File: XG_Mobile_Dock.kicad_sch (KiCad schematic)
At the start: 21 parts, among them J1 5-1775443-8, J17 8730, J2 20455-040E-76, J3 20455-040E-76, J4 3-2362375-4, J7 Conn_02x10_Odd_Even, J8 Conn_02x10_Odd_Even

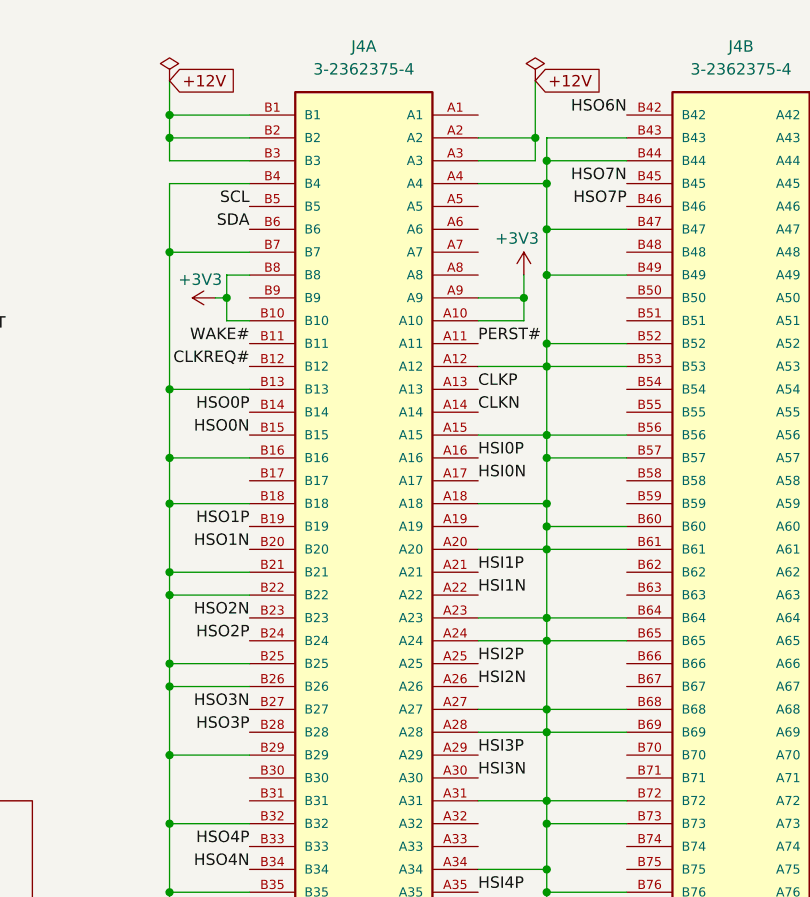
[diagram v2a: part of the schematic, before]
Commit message: Replace TH PCI-E slot with SMD
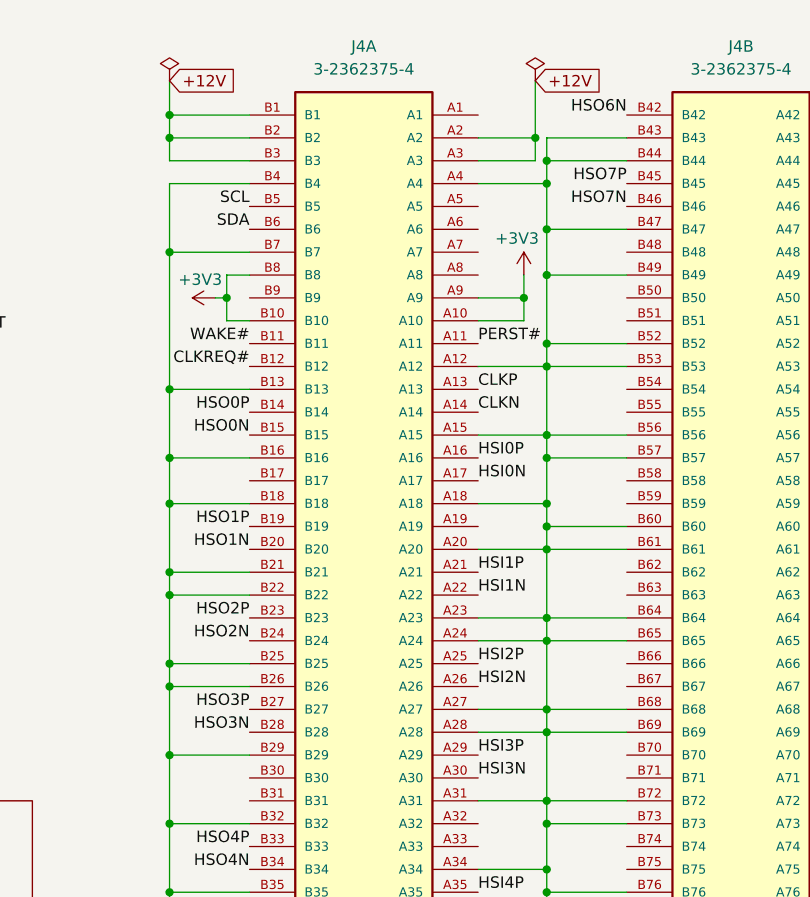
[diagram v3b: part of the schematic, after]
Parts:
- J4: footprint SAMTEC_PCIE-164-02-F-D-TH-TR:SAMTEC_PCIE-164-02-F-D-TH-TR -> 3113-113T:CONN-SMD_164P-P1.00-V_3133; LCSC C404116 -> C404104; Part_Number 3183-10203P1T -> 3113-113T
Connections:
- net HSO2N: now also J4.B24; no longer J4.B23
- net HSO2P: now also J4.B23; no longer J4.B24
- net HSO3N: now also J4.B28; no longer J4.B27
- net HSO3P: now also J4.B27; no longer J4.B28
- net HSO7N: now also J4.B46; no longer J4.B45
- net HSO7P: now also J4.B45; no longer J4.B46
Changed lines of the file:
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@@
 		)
 	)
-	(label "HSO3N"
+	(label "HSO3P"
 		(at 198.12 93.98 180)
 		(fields_autoplaced yes)
@@
 		)
 	)
-	(label "HSO2N"
+	(label "HSO2P"
 		(at 198.12 83.82 180)
 		(fields_autoplaced yes)
@@
 		)
 	)
-	(label "HSO3P"
+	(label "HSO3N"
 		(at 198.12 96.52 180)
 		(fields_autoplaced yes)
@@
 		)
 	)
-	(label "HSO7P"
+	(label "HSO7N"
 		(at 240.03 38.1 180)
 		(fields_autoplaced yes)
@@
 		)
 	)
-	(label "HSO7N"
+	(label "HSO7P"
 		(at 240.03 35.56 180)
 		(fields_autoplaced yes)
@@
 		)
 	)
-	(label "HSO2P"
+	(label "HSO2N"
 		(at 198.12 86.36 180)
 		(fields_autoplaced yes)
@@
 			)
 		)
-		(property "Footprint" "SAMTEC_PCIE-164-02-F-D-TH-TR:SAMTEC_PCIE-164-02-F-D-TH-TR"
+		(property "Footprint" "3113-113T:CONN-SMD_164P-P1.00-V_3133"
 			(at 252.73 78.74 0)
 			(effects
@@
 			)
 		)
-		(property "Part_Number" "3183-10203P1T"
+		(property "Part_Number" "3113-113T"
 			(at 252.73 78.74 0)
 			(effects
@@
 			)
 		)
-		(property "LCSC" "C404116"
+		(property "LCSC" "C404104"
 			(at 252.73 78.74 0)
 			(effects
@@
 			)
 		)
-		(property "Footprint" "SAMTEC_PCIE-164-02-F-D-TH-TR:SAMTEC_PCIE-164-02-F-D-TH-TR"
+		(property "Footprint" "3113-113T:CONN-SMD_164P-P1.00-V_3133"
 			(at 210.82 78.74 0)
 			(effects
@@
 			)
 		)
-		(property "Part_Number" "3183-10203P1T"
+		(property "Part_Number" "3113-113T"
 			(at 210.82 78.74 0)
 			(effects
@@
 			)
 		)
-		(property "LCSC" "C404116"
+		(property "LCSC" "C404104"
 			(at 210.82 78.74 0)
 			(effects

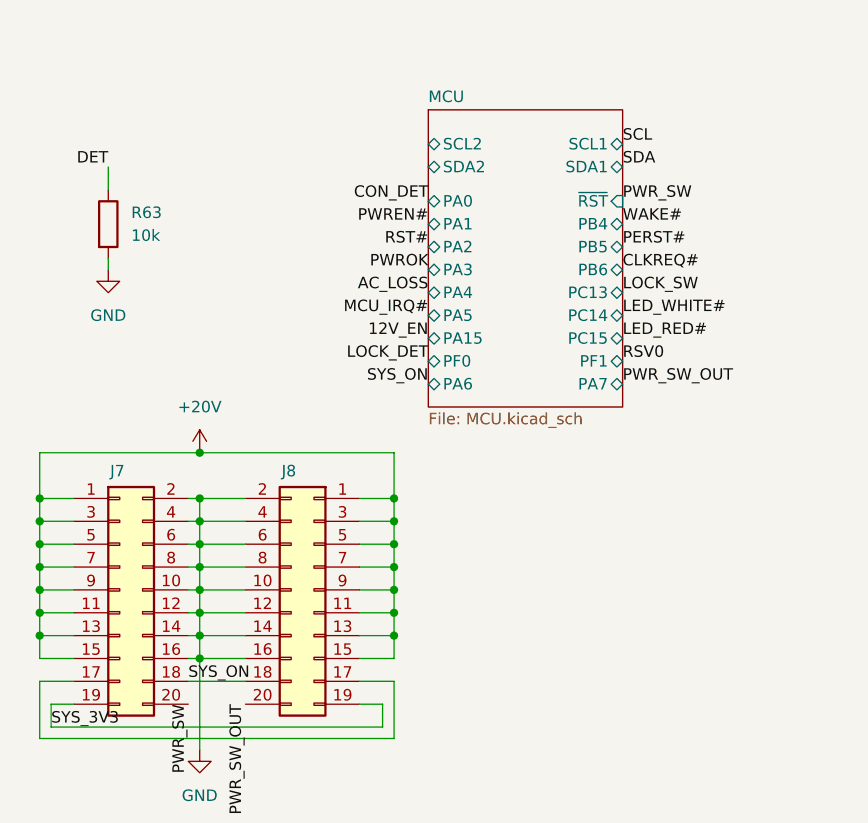
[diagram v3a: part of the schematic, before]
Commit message: Add external board detect pin to MCU
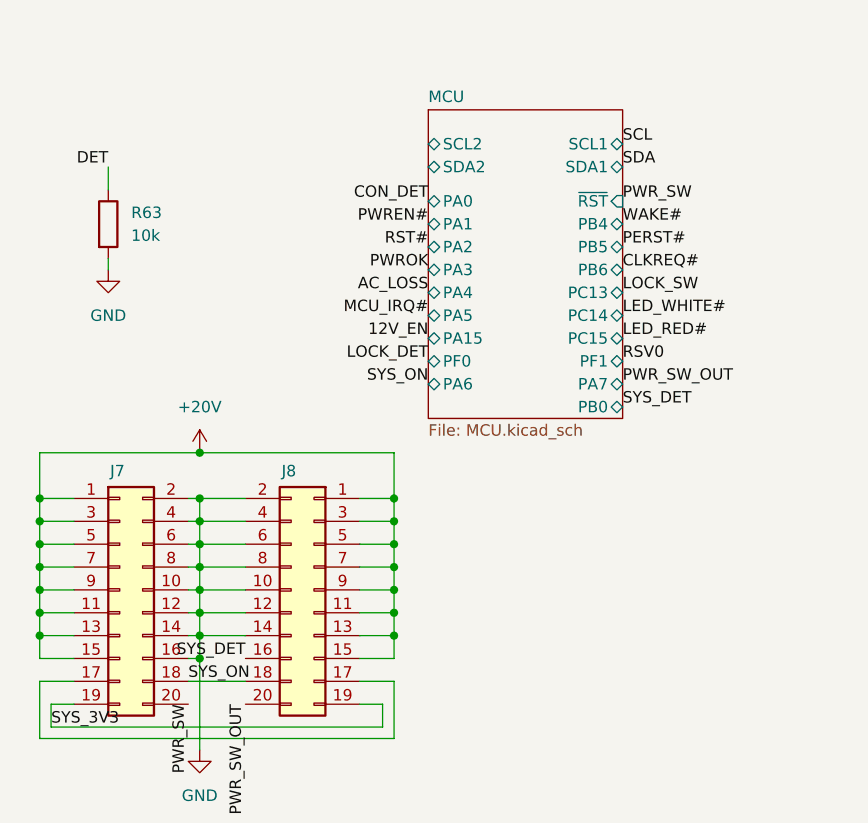
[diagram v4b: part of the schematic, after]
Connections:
- net GND: no longer J8.16 (Pin_16)
- new net SYS_DET: J8.16 (Pin_16)
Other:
- sheet MCU ports: added PB0; removed none
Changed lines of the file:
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@@
 	(wire
 		(pts
-			(xy 111.76 82.55) (xy 116.84 82.55)
-		)
-		(stroke
-			(width 0)
-			(type default)
-		)
-	)
-	(wire
-		(pts
 			(xy 46.99 67.31) (xy 46.99 74.93)
 		)
@@
 		)
 	)
+	(label "SYS_DET"
+		(at 116.84 82.55 180)
+		(fields_autoplaced yes)
+		(effects
+			(font
+				(size 1.27 1.27)
+			)
+			(justify right bottom)
+		)
+	)
 	(label "HSI6P"
 		(at 265.43 30.48 0)
@@
 		)
 	)
+	(label "SYS_DET"
+		(at 158.75 54.61 0)
+		(fields_autoplaced yes)
+		(effects
+			(font
+				(size 1.27 1.27)
+			)
+			(justify left bottom)
+		)
+	)
 	(label "HSO5P"
 		(at 198.12 119.38 180)
@@
 	(sheet
 		(at 137.16 21.59)
-		(size 21.59 33.02)
+		(size 21.59 34.29)
 		(fields_autoplaced yes)
 		(stroke
@@
 		)
 		(property "Sheetfile" "MCU.kicad_sch"
-			(at 137.16 55.1946 0)
+			(at 137.16 56.4646 0)
 			(effects
 				(font
@@
 			(effects
 				(font
+					(size 1.27 1.27)
+				)
+				(justify right)
+			)
+		)
+		(pin "PB0" bidirectional
+			(at 158.75 54.61 0)
+			(effects
+				(font

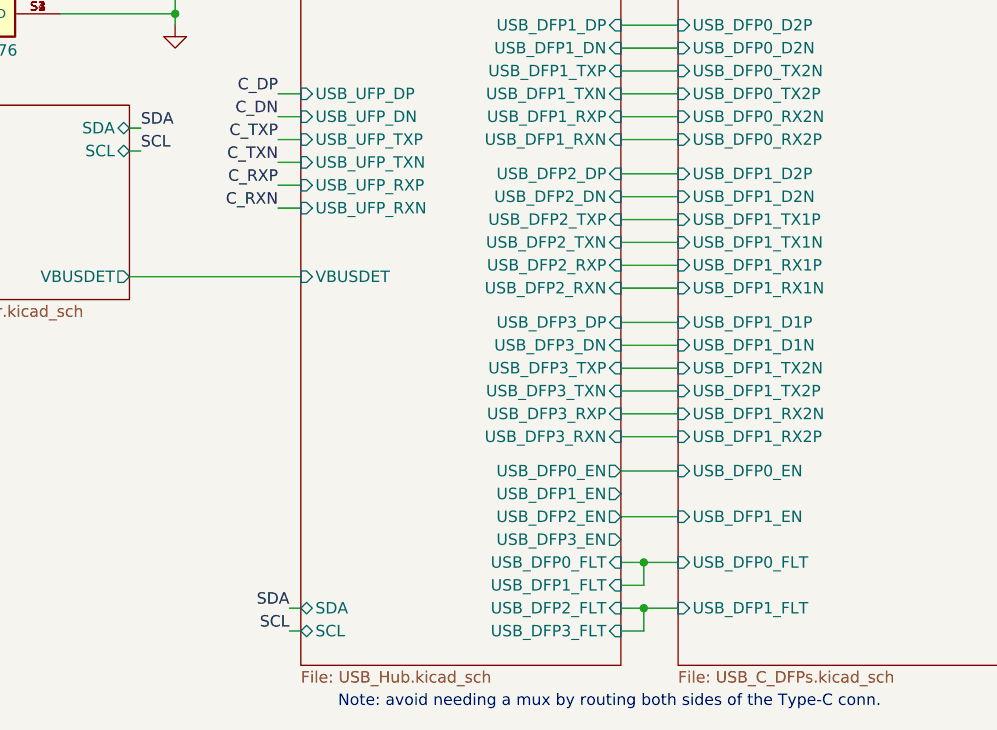
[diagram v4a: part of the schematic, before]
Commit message: pcb: redid layout for USB hub
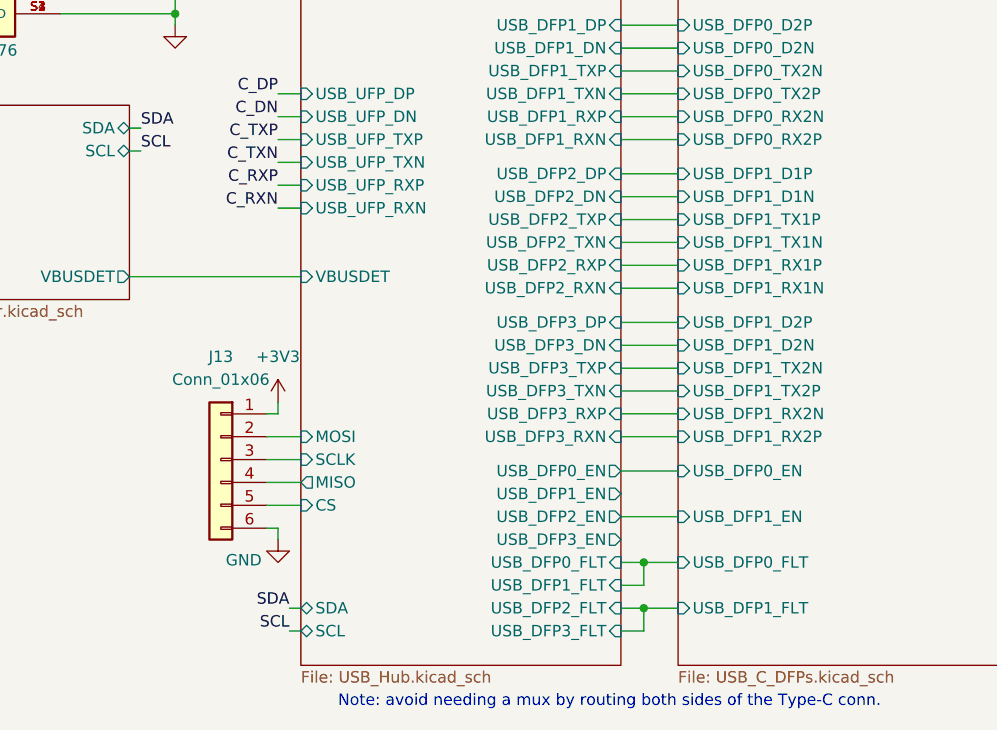
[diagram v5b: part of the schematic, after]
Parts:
- added J13: Conn_01x06, Connector_PinHeader_2.54mm:PinHeader_1x06_P2.54mm_Vertical, symbol Connector_Generic:Conn_01x06
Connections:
- net +3V3: now also J13.1 (Pin_1)
- net GND: now also J13.6 (Pin_6)
- new net USB Hub/CS: J13.5 (Pin_5)
- new net USB Hub/MISO: J13.4 (Pin_4)
- new net USB Hub/MOSI: J13.2 (Pin_2)
- new net USB Hub/SCLK: J13.3 (Pin_3)
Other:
- sheet USB Hub ports: added CS, MISO, MOSI, SCLK; removed none

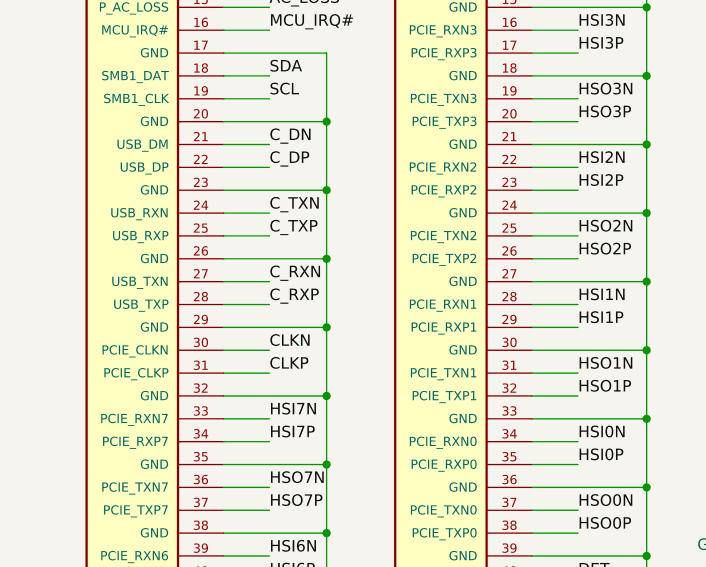
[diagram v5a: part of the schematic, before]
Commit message: pcb: updated all via sizes to >= 0.4/0.3
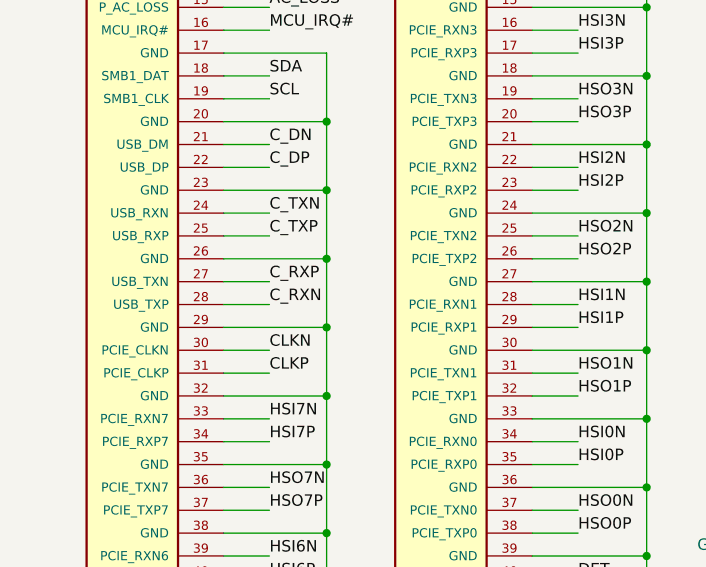
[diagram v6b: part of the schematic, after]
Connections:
- net C_RXN: now also J3.28 (USB_TXP); no longer J3.27 (USB_TXN)
- net C_RXP: now also J3.27 (USB_TXN); no longer J3.28 (USB_TXP)
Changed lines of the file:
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@@
 		)
 	)
-	(label "C_RXP"
+	(label "C_RXN"
 		(at 40.64 87.63 0)
 		(fields_autoplaced yes)
@@
 		)
 	)
-	(label "C_RXN"
+	(label "C_RXP"
 		(at 40.64 85.09 0)
 		(fields_autoplaced yes)

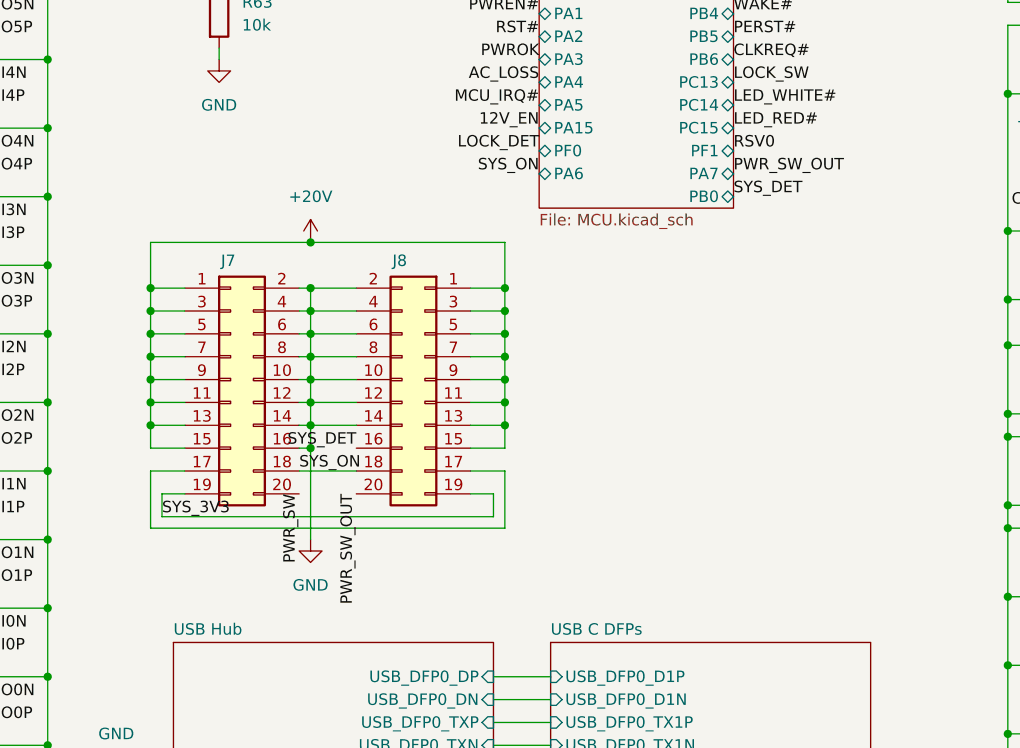
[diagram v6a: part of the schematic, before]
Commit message: pcb: replaced 20P slot with mirrored connector
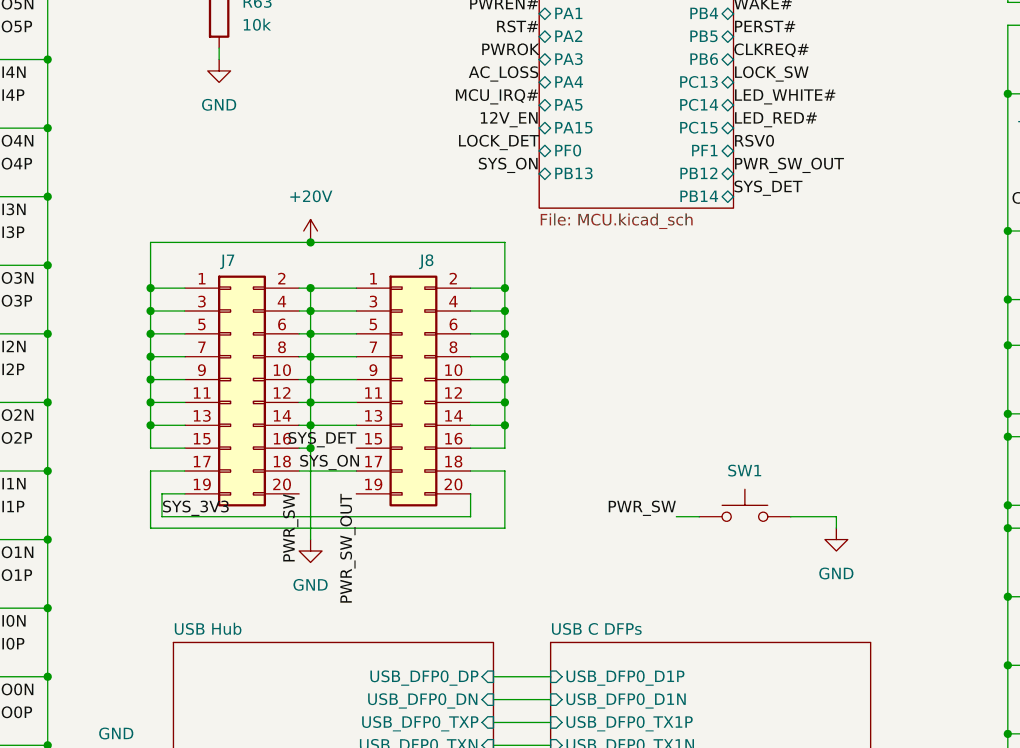
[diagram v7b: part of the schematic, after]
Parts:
- added SW1: SW_Push, Button_Switch_SMD:SW_SPST_SKQG_WithStem, symbol Switch:SW_Push
- J17: LCSC (none) -> C7200700; Part_Number (none) -> 8730
- J7: LCSC 5-5530843-0 -> C305933
- J8: footprint XG_Mobile:20P_Slot_Power -> 5-5530843-0:5-5530843-0; LCSC (none) -> C305933; Part_Number (none) -> 5-5530843-0; now in the parts list
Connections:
- net +20V: now also J8.10 (Pin_10), J8.12 (Pin_12), J8.14 (Pin_14), J8.16 (Pin_16), J8.2 (Pin_2), J8.4 (Pin_4), J8.6 (Pin_6), J8.8 (Pin_8); no longer J8.1 (Pin_1), J8.11 (Pin_11), J8.13 (Pin_13), J8.15 (Pin_15), J8.3 (Pin_3), J8.5 (Pin_5), J8.7 (Pin_7), J8.9 (Pin_9)
- net GND: now also J8.1 (Pin_1), J8.11 (Pin_11), J8.13 (Pin_13), J8.3 (Pin_3), J8.5 (Pin_5), J8.7 (Pin_7), J8.9 (Pin_9), SW1.2; no longer J8.10 (Pin_10), J8.12 (Pin_12), J8.14 (Pin_14), J8.2 (Pin_2), J8.4 (Pin_4), J8.6 (Pin_6), J8.8 (Pin_8)
- net PWR_SW: now also SW1.1
- net PWR_SW_OUT: now also J8.19 (Pin_19); no longer J8.20 (Pin_20)
- net SYS_3V3: now also J8.20 (Pin_20); no longer J8.19 (Pin_19)
- net SYS_DET: now also J8.15 (Pin_15); no longer J8.16 (Pin_16)
- net SYS_ON: now also J8.17 (Pin_17); no longer J8.18 (Pin_18)
- net at J7.17 (Pin_17): now also J8.18 (Pin_18); no longer J8.17 (Pin_17)
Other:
- sheet MCU ports: added PB12, PB13, PB14; removed PA6, PA7, PB0

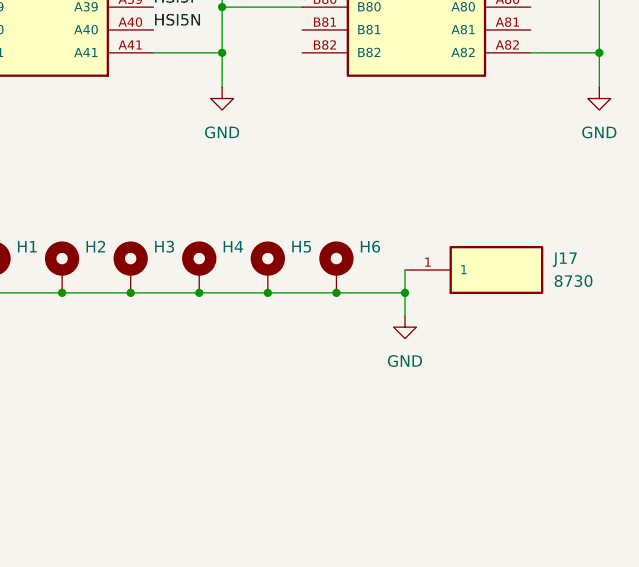
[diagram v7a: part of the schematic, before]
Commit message: pcb: improve thermal reliefs for pth
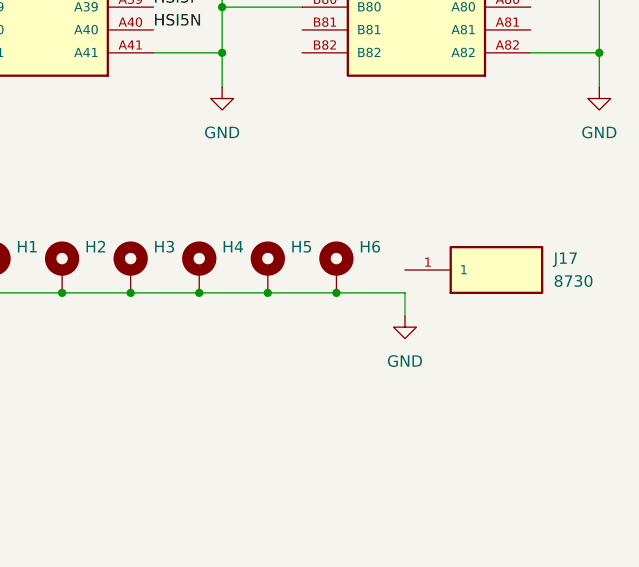
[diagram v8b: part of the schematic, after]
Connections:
- net GND: no longer J17.1
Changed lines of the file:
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@@
 	)
 	(junction
-		(at 251.46 156.21)
-		(diameter 0)
-		(color 0 0 0 0)
-	)
-	(junction
 		(at 93.98 74.93)
 		(diameter 0)
@@
 		)
 		(stroke
-			(width 0)
-			(type default)
-		)
-	)
-	(wire
-		(pts
-			(xy 251.46 153.67) (xy 251.46 156.21)
-		)
-		(stroke
